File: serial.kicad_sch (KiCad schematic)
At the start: 12 parts, among them J401 USB serial, U401 USBLC6-2SC6, U402 XC6206PxxxMR, U403 CH330N

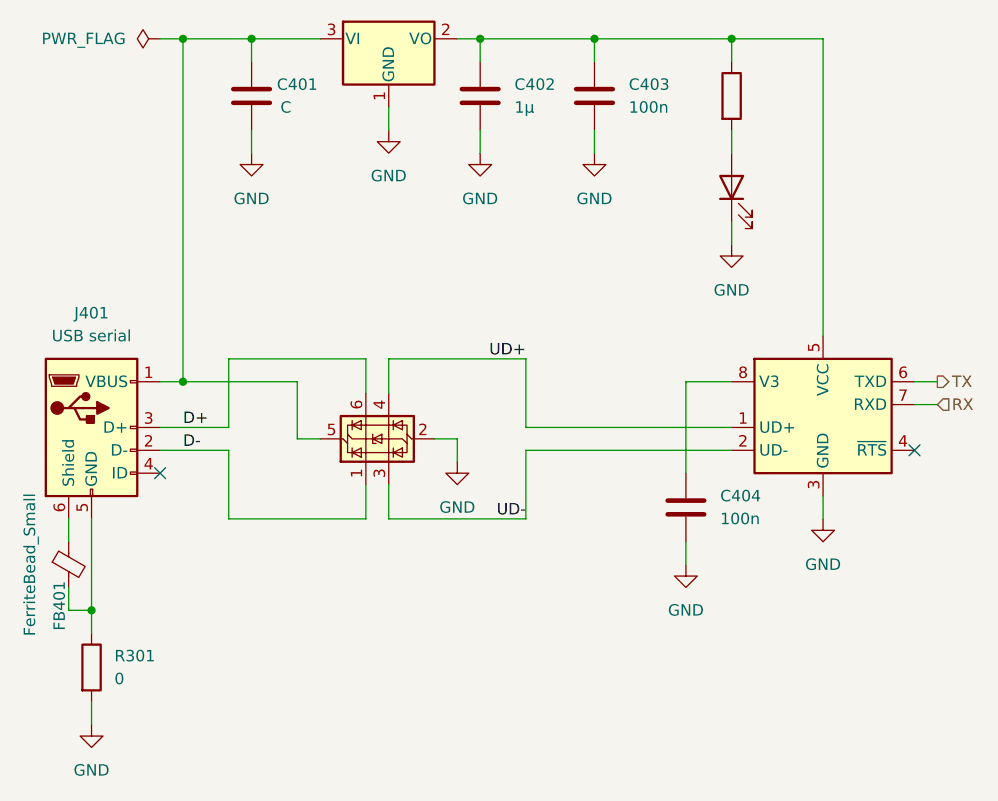
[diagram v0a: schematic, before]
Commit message: Fix USB
Signed-off-by: Benedikt Spranger <b.spranger@linutronix.de>
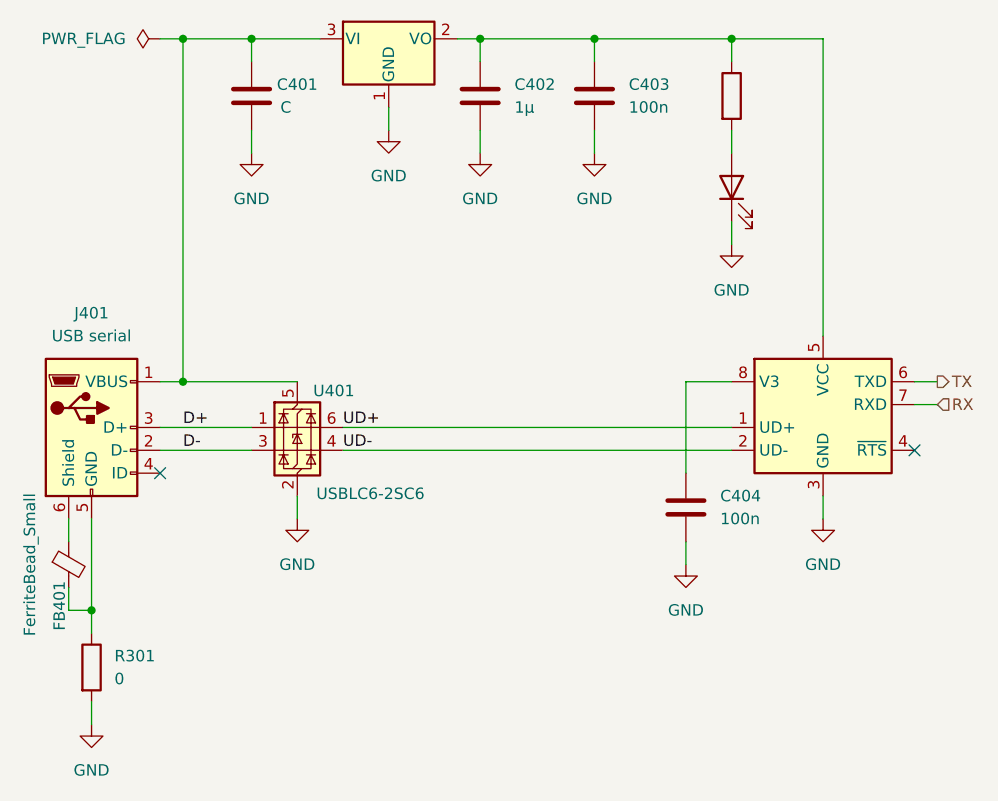
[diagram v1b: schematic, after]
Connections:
- net D+: now also U401.1 (I/O1); no longer U401.6 (I/O1)
- net D-: now also U401.3 (I/O2); no longer U401.1 (I/O1)
- net UD+: now also U401.6 (I/O1); no longer U401.4 (I/O2)
- net UD-: now also U401.4 (I/O2); no longer U401.3 (I/O2)
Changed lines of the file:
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@@
-	(wire
-		(pts
-			(xy 142.24 107.95) (xy 144.78 107.95)
-		)
-		(stroke
-			(width 0)
-			(type default)
-		)
-	)
 	(wire
 		(pts
@@
 	(wire
 		(pts
-			(xy 119.38 116.84) (xy 134.62 116.84)
-		)
-		(stroke
-			(width 0)
-			(type default)
-		)
-	)
-	(wire
-		(pts
 			(xy 160.02 63.5) (xy 160.02 66.04)
 		)
@@
 	(wire
 		(pts
-			(xy 119.38 99.06) (xy 134.62 99.06)
-		)
-		(stroke
-			(width 0)
-			(type default)
-		)
-	)
-	(wire
-		(pts
-			(xy 111.76 106.68) (xy 119.38 106.68)
+			(xy 111.76 106.68) (xy 121.92 106.68)
 		)
 		(stroke
@@
 	(wire
 		(pts
-			(xy 144.78 107.95) (xy 144.78 110.49)
-		)
-		(stroke
-			(width 0)
-			(type default)
-		)
-	)
-	(wire
-		(pts
 			(xy 101.6 127) (xy 104.14 127)
 		)
@@
 	(wire
 		(pts
-			(xy 137.16 116.84) (xy 152.4 116.84)
-		)
-		(stroke
-			(width 0)
-			(type default)
-		)
-	)
-	(wire
-		(pts
-			(xy 137.16 99.06) (xy 152.4 99.06)
-		)
-		(stroke
-			(width 0)
-			(type default)
-		)
-	)
-	(wire
-		(pts
 			(xy 121.92 73.66) (xy 121.92 76.2)
 		)
@@
 	(wire
 		(pts
-			(xy 111.76 109.22) (xy 119.38 109.22)
+			(xy 111.76 109.22) (xy 121.92 109.22)
 		)
 		(stroke
@@
 	(wire
 		(pts
-			(xy 152.4 109.22) (xy 175.26 109.22)
-		)
-		(stroke
-			(width 0)
-			(type default)
-		)
-	)
-	(wire
-		(pts
 			(xy 147.32 63.5) (xy 147.32 66.04)
 		)
@@
 	(wire
 		(pts
-			(xy 119.38 106.68) (xy 119.38 99.06)
+			(xy 132.08 106.68) (xy 175.26 106.68)
 		)
 		(stroke
@@
 	(wire
 		(pts
-			(xy 152.4 99.06) (xy 152.4 106.68)
-		)
-		(stroke
-			(width 0)
-			(type default)
-		)
-	)
-	(wire
-		(pts
-			(xy 137.16 99.06) (xy 137.16 102.87)
-		)
-		(stroke
-			(width 0)
-			(type default)
-		)
-	)
-	(wire
-		(pts
 			(xy 114.3 101.6) (xy 127 101.6)
 		)
@@
 	(wire
 		(pts
-			(xy 152.4 106.68) (xy 175.26 106.68)
-		)
-		(stroke
-			(width 0)
-			(type default)
-		)
-	)
-	(wire
-		(pts
-			(xy 127 101.6) (xy 127 107.95)
+			(xy 127 114.3) (xy 127 116.84)
 		)
 		(stroke
@@
 	(wire
 		(pts
-			(xy 134.62 113.03) (xy 134.62 116.84)
-		)
-		(stroke
-			(width 0)
-			(type default)
-		)
-	)
-	(wire
-		(pts
-			(xy 137.16 113.03) (xy 137.16 116.84)
-		)
-		(stroke
-			(width 0)
-			(type default)
-		)
-	)
-	(wire
-		(pts
-			(xy 119.38 109.22) (xy 119.38 116.84)
-		)
-		(stroke
-			(width 0)
-			(type default)
-		)
-	)
-	(wire
-		(pts
 			(xy 104.14 116.84) (xy 104.14 127)
 		)
@@
 	(wire
 		(pts
-			(xy 152.4 116.84) (xy 152.4 109.22)
-		)
-		(stroke
-			(width 0)
-			(type default)
-		)
-	)
-	(wire
-		(pts
 			(xy 111.76 63.5) (xy 114.3 63.5)
 		)
@@
 	(wire
 		(pts
-			(xy 134.62 99.06) (xy 134.62 102.87)
-		)
-		(stroke
-			(width 0)
-			(type default)
-		)
-	)
-	(wire
-		(pts
-			(xy 127 107.95) (xy 129.54 107.95)
-		)
-		(stroke
-			(width 0)
-			(type default)
-		)
-	)
-	(wire
-		(pts
 			(xy 147.32 63.5) (xy 160.02 63.5)
 		)
@@
 		)
 	)
+	(wire
+		(pts
+			(xy 132.08 109.22) (xy 175.26 109.22)
+		)
+		(stroke
+			(width 0)
+			(type default)
+		)
+	)
 	(label "UD-"
-		(at 152.4 116.84 180)
+		(at 132.08 109.22 0)
 		(fields_autoplaced yes)
 		(effects
@@
 				(size 1.27 1.27)
 			)
-			(justify right bottom)
+			(justify left bottom)
 		)
 	)
@@
 	)
 	(label "UD+"
-		(at 152.4 99.06 180)
+		(at 132.08 106.68 0)
 		(fields_autoplaced yes)
 		(effects
@@
 				(size 1.27 1.27)
 			)
-			(justify right bottom)
+			(justify left bottom)
 		)
 	)
@@
 	(symbol
 		(lib_id "power:GND")
-		(at 144.78 110.49 0)
+		(at 127 116.84 0)
 		(unit 1)
 		(exclude_from_sim no)
@@
 		(fields_autoplaced yes)
 		(property "Reference" "#PWR0404"
-			(at 144.78 116.84 0)
+			(at 127 123.19 0)
 			(effects
 				(font
@@
 		)
 		(property "Value" "GND"
-			(at 144.78 115.57 0)
+			(at 127 121.92 0)
 			(effects
 				(font
@@
 		)
 		(property "Footprint" ""
-			(at 144.78 110.49 0)
+			(at 127 116.84 0)
 			(effects
 				(font
@@
 		)
 		(property "Datasheet" ""
-			(at 144.78 110.49 0)
+			(at 127 116.84 0)
 			(effects
 				(font
@@
 		)
 		(property "Description" "Power symbol creates a global label with name \"GND\" , ground"
-			(at 144.78 110.49 0)
+			(at 127 116.84 0)
 			(effects
 				(font
@@
 	(symbol
 		(lib_id "Power_Protection:USBLC6-2SC6")
-		(at 134.62 107.95 90)
+		(at 127 106.68 0)
 		(unit 1)
 		(exclude_from_sim no)
@@
 		(on_board yes)
 		(dnp no)
-		(fields_autoplaced yes)
 		(property "Reference" "U401"
-			(at 134.62 107.95 0)
-			(effects
-				(font
-					(size 1.27 1.27)
-				)
-				(hide yes)
+			(at 131.064 102.616 0)
+			(effects
+				(font
+					(size 1.27 1.27)
+				)
 			)
 		)
 		(property "Value" "USBLC6-2SC6"
-			(at 134.62 107.95 0)
-			(effects
-				(font
-					(size 1.27 1.27)
-				)
-				(hide yes)
+			(at 135.128 114.046 0)
+			(effects
+				(font
+					(size 1.27 1.27)
+				)
 			)
 		)
 		(property "Footprint" "Package_TO_SOT_SMD:SOT-23-6"
-			(at 147.32 107.95 0)
+			(at 127 119.38 0)
 			(effects
 				(font
@@
 		)
 		(property "Datasheet" "https://www.st.com/resource/en/datasheet/usblc6-2.pdf"
-			(at 134.62 107.95 0)
+			(at 127 106.68 0)
 			(effects
 				(font
@@
 		)
 		(property "Description" "Very low capacitance ESD protection diode, 2 data-line, SOT-23-6"
-			(at 134.62 107.95 0)
+			(at 127 106.68 0)
 			(effects
 				(font
@@
 		)
 		(property "assemble" "y"
-			(at 134.62 107.95 0)
+			(at 127 106.68 0)
 			(effects
 				(font
@@
 		)
 		(property "SupplLink" "https://jlcpcb.com/partdetail/TechPublic-USBLC62SC6/C2827654"
-			(at 134.62 107.95 0)
+			(at 127 106.68 0)
 			(effects
 				(font
@@
 		)
 		(property "digikey#" ""
-			(at 134.62 107.95 0)
+			(at 127 106.68 0)
 			(effects
 				(font
@@
 		)
 		(property "tme#" ""
-			(at 134.62 107.95 0)
+			(at 127 106.68 0)
 			(effects
 				(font
@@
 		)
 		(property "Long Description" "SOT-23-6 ESD Protection Devices ROHS"
-			(at 134.62 107.95 0)
+			(at 127 106.68 0)
 			(effects
 				(font
@@
 		)
 		(property "MF" "TECH PUBLIC"
-			(at 134.62 107.95 0)
+			(at 127 106.68 0)
 			(effects
 				(font
@@
 		)
 		(property "MP" "USBLC6-2SC6"
-			(at 134.62 107.95 0)
+			(at 127 106.68 0)
 			(effects
 				(font
@@
 		)
 		(property "lcsc#" "C2827654"
-			(at 134.62 107.95 0)
+			(at 127 106.68 0)
 			(effects
 				(font
@@
 		)
 		(property "Source" "JLCPCB"
-			(at 134.62 107.95 0)
-			(effects
-				(font
+			(at 127 106.68 0)
+			(effects
+				(font

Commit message: Update to KiCAD 9.x
Signed-off-by: Benedikt Spranger <b.spranger@linutronix.de>
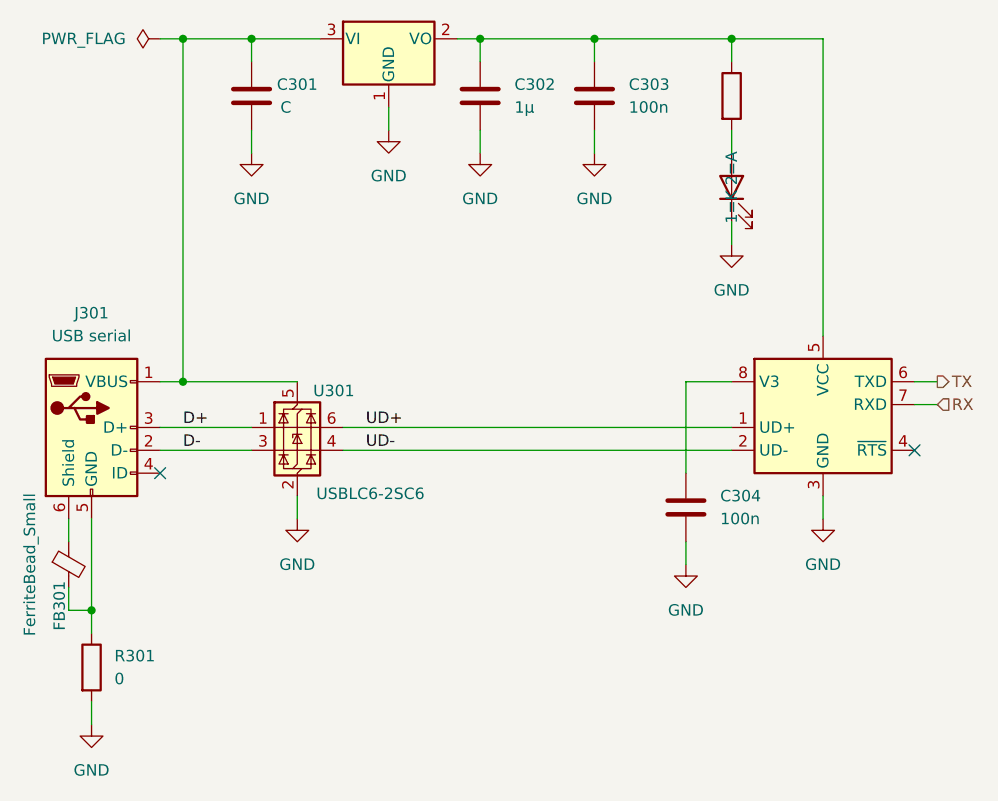
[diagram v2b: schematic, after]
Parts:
- renumbered C401 to C301, C402 to C302, C403 to C303, C404 to C304, D401 to D301, FB401 to FB301, J401 to J301, R402 to R302, U401 to U301, U402 to U302, U403 to U303

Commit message: Rework Input selection
Signed-off-by: Benedikt Spranger <b.spranger@linutronix.de>
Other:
- company: Linutronix GmbH / Benedikt Spranger -> Eurovibes Benedikt Spranger
- title: Fair Demo - Input shield -> Akkupack NG
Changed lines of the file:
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@@
 	(paper "A4")
 	(title_block
-		(title "Fair Demo - Input shield")
-		(date "2024-01-14")
+		(title "Akkupack NG")
+		(date "2024-05-10")
 		(rev "0.1")
-		(company "Linutronix GmbH / Benedikt Spranger")
+		(company "Eurovibes Benedikt Spranger")
 		(comment 1 "SPDX-License-Identifier: CERN-OHL-S-2.0")
 		(comment 2 "https://ohwr.org/cern_ohl_s_v2.txt")
@@
 		(dnp no)
 		(fields_autoplaced yes)
-		(property "Reference" "#PWR0303"
+		(property "Reference" "#PWR0304"
 			(at 137.16 80.01 0)
 			(effects
@@
 			(project "akkupack-ng"
 				(path "/28c14643-513c-46b6-b18d-27cb3c7eee92/de76c23a-5b99-4def-922c-07fd05553b7c/6dcc1ff5-8384-404f-a673-016d43e5259c"
-					(reference "#PWR0303")
+					(reference "#PWR0304")
 					(unit 1)
 				)
 				(path "/28c14643-513c-46b6-b18d-27cb3c7eee92/de76c23a-5b99-4def-922c-07fd05553b7c/b42c4ae4-142a-4071-85c3-0a5227412cad"
-					(reference "#PWR0403")
+					(reference "#PWR0404")
 					(unit 1)
 				)
@@
 		(dnp no)
 		(fields_autoplaced yes)
-		(property "Reference" "#PWR0304"
+		(property "Reference" "#PWR0303"
 			(at 127 123.19 0)
 			(effects
@@
 			(project "akkupack-ng"
 				(path "/28c14643-513c-46b6-b18d-27cb3c7eee92/de76c23a-5b99-4def-922c-07fd05553b7c/6dcc1ff5-8384-404f-a673-016d43e5259c"
-					(reference "#PWR0304")
+					(reference "#PWR0303")
 					(unit 1)
 				)
 				(path "/28c14643-513c-46b6-b18d-27cb3c7eee92/de76c23a-5b99-4def-922c-07fd05553b7c/b42c4ae4-142a-4071-85c3-0a5227412cad"
-					(reference "#PWR0404")
-					(unit 1)
-				)
+					(reference "#PWR0403")
+					(unit 1)
+				)
